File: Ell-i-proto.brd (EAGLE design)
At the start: 99 x 53.3 mm, 145 parts, among them J1 FTDI-SER-6, J10 PJ-102AX, J2 PWMH, J3 PWR, J4 PWML, J5 ANAL, J6 SPI, J7 COMM, J8 ANAH, J9 RJ45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

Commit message: all lines somehow routed and seem to fit to the board, some parts updated, etc
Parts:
- removed Q5: (no value), crystal:SM49
- added C45, C46, C47, C48: 22u, ell-i:0805
- C13: value 10uF -> 22uF; device ell-i:0603 -> ell-i:0805
- C34: value 100uF -> 22u; device rcl:C1206 -> ell-i:0805
- H1, H2, H3, H4, H5, H6: value MOUNT-HOLE3.2 -> MOUNT_HOLE; device holes:3,2 -> ell-i:MOUNT_HOLE
- J1: value FTDI-SER-6 -> TSM-106-01-L-SH; device ell-i:FTDI-SER-6 -> ell-i:TSM-106-01-L-SH
- J10: value PJ-102AX -> KLDX-SMT2-0202; device ell-i:PJ-102A -> ell-i:KLDX-SMT2-0202
- J9: device ell-i:43860-0001 -> ell-i:85502-5008
- S1: value B3SL-10X2P -> EVQQ2/P0; device ell-i:B3SL-10X2P -> ell-i:EVQQ2/P0
- Y1: value 8MHz -> (none); device ell-i:XTAL3225 -> crystal:SM49
- moved PC15 56.4 mm to (68.4, 16.8)
- moved PC14 54.7 mm to (67.3, 17.9)
- moved VPORTN 45.3 mm to (14.5, 19.1)
- moved PC12 44.9 mm to (76.9, 23.4)
- moved V+ 44.6 mm to (16.9, 18.4)
- moved PF5 40.7 mm to (72.3, 6.63)
- moved PF4 39.1 mm to (71.5, 6.93)
- moved TP3 35.9 mm to (33.7, 22.8)
- moved FID2 35.5 mm to (80.9, 38.8)
- moved PB2 30.8 mm to (78.0, 6.73)
- moved R21 30.6 mm to (58.5, 18.4)
- moved D12 28.7 mm to (56.2, 10.1), turned to 270 degrees
- moved C37 28.5 mm to (59.0, 20.0), turned to 90 degrees
- moved C26 24.1 mm to (20.3, 28.0), turned to 180 degrees
- moved TP10 23.4 mm to (4.57, 28.4)
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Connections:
- net +5V: now also C45.1, C46.1, C47.1, C48.1
- net GND: now also J10.1; no longer J10.3
- net GNDI: now also C45.2, C46.2, C47.2, C48.2, J1.6; no longer J1.GND, Y1.2, Y1.4
- net N$6: now also J1.5; no longer J1.-CTS
- net N184903: now also J10.3@1, J10.3@2; no longer J10.1
- net N205481: now also Y1.1; no longer Y1.3
- net NDSR2: now also J1.1; no longer J1.-RTS
- net PE: now also J9.S1, J9.S2
- net PF0: now also Y1.2; no longer Y1.1
- net RX2: now also J1.3; no longer J1.TXD
- net TX2: now also J1.2; no longer J1.RXD
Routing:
- net SCL2: track 0.00 -> 88.3 mm, vias 0 -> 1
- net SDA2: track 0.00 -> 84.5 mm, vias 0 -> 1
- net IO9: track 0.00 -> 73.3 mm, vias 0 -> 3
- net IO8: track 0.00 -> 70.6 mm, vias 0 -> 3
- net RX2: track 23.9 -> 93.7 mm, vias 1 -> 3
- net MOSI1: track 0.00 -> 68.5 mm, vias 0 -> 2
- net SCK1: track 0.00 -> 68.0 mm, vias 0 -> 2
- net MISO1: track 0.00 -> 66.4 mm, vias 0 -> 2
- net IO4: track 0.00 -> 66.0 mm, vias 0 -> 2
- net SCK_ETH: track 0.00 -> 64.3 mm, vias 0 -> 2
- net NSS_ETH: track 0.00 -> 64.2 mm, vias 0 -> 2
- net IO3: track 0.00 -> 63.9 mm, vias 0 -> 2
- net IO7: track 0.00 -> 62.1 mm, vias 0 -> 3
- net IO2: track 0.00 -> 60.5 mm, vias 0 -> 2
- net NRES: track 47.7 -> 107.9 mm, vias 1 -> 8
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- added copper zone on layer 16, net N23620

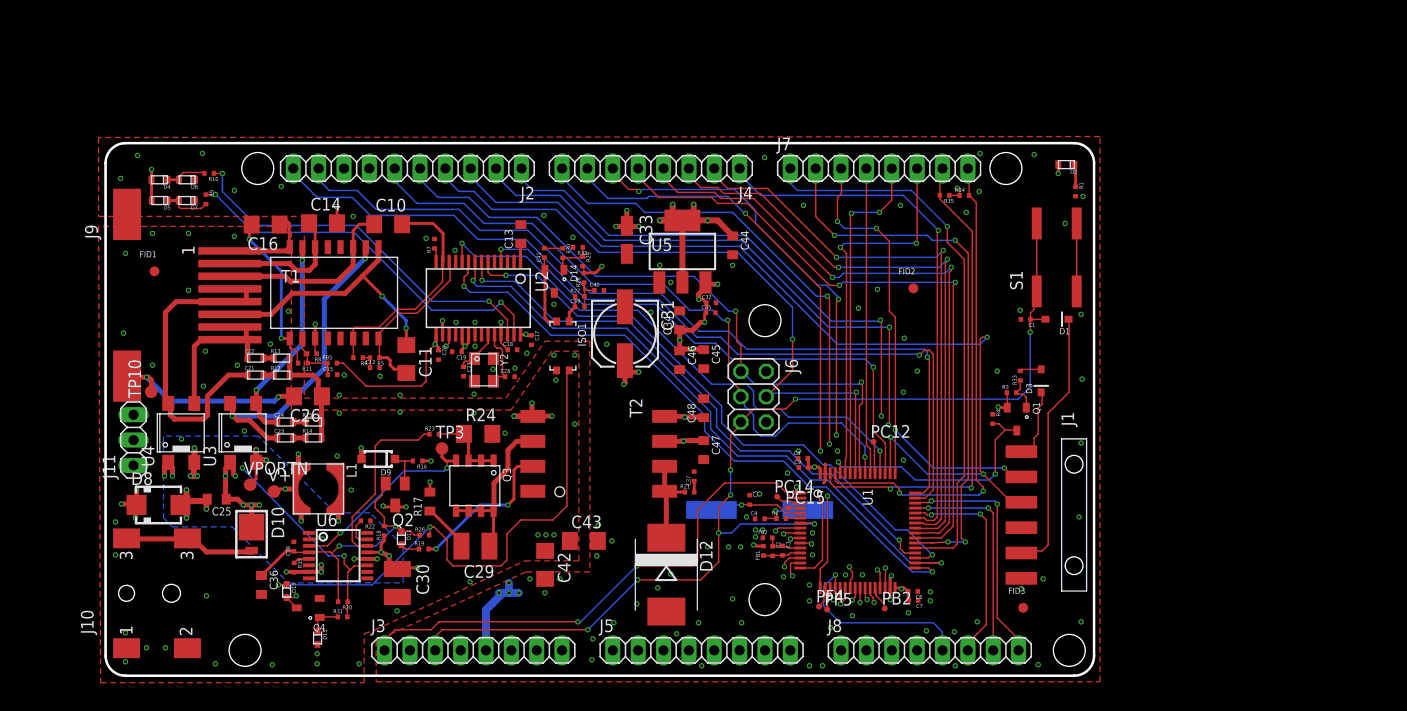
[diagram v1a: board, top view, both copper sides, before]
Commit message: net class & track width updates
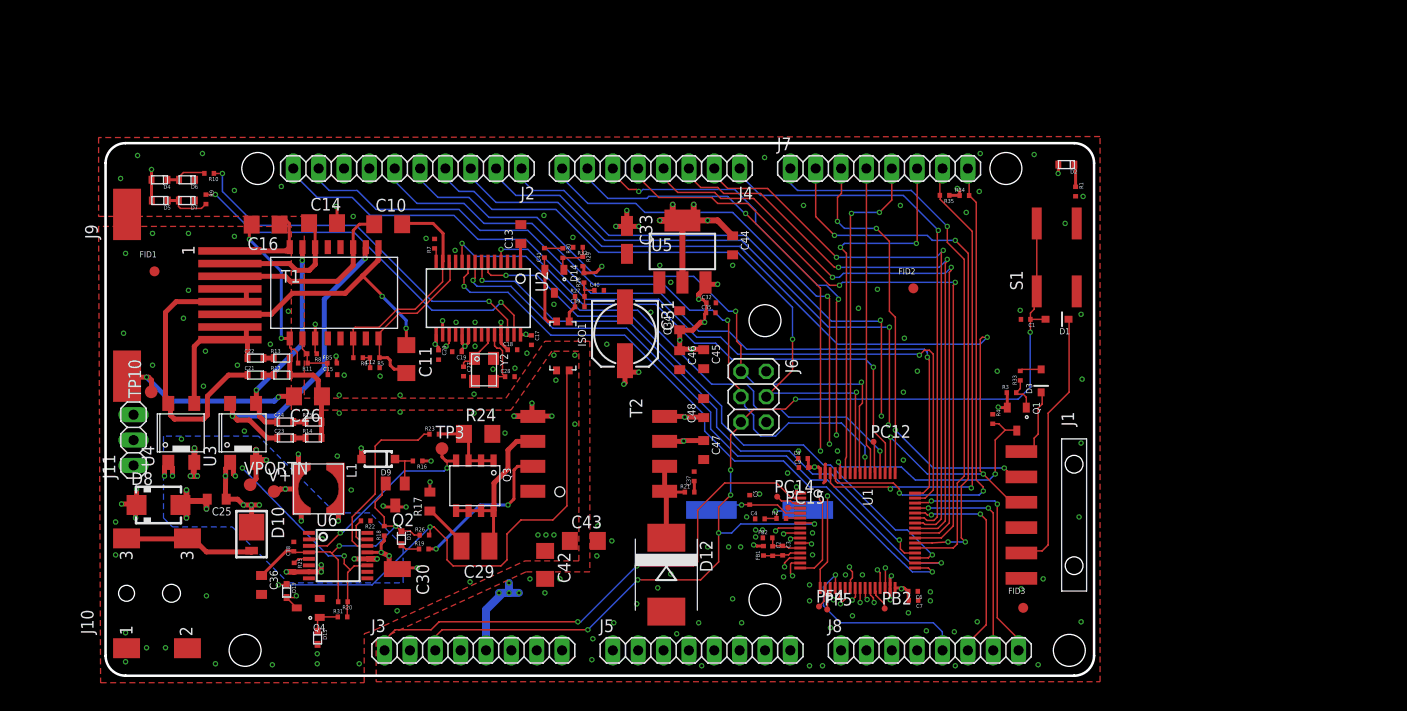
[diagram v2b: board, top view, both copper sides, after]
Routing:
- net +3V3: track 69.6 -> 54.9 mm, vias 19 -> 20
- net GNDI: track 11.0 -> 4.22 mm
- net N23620: track 25.7 -> 24.4 mm
- net GND: vias 40 -> 41

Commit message: gnd planes optimized etc
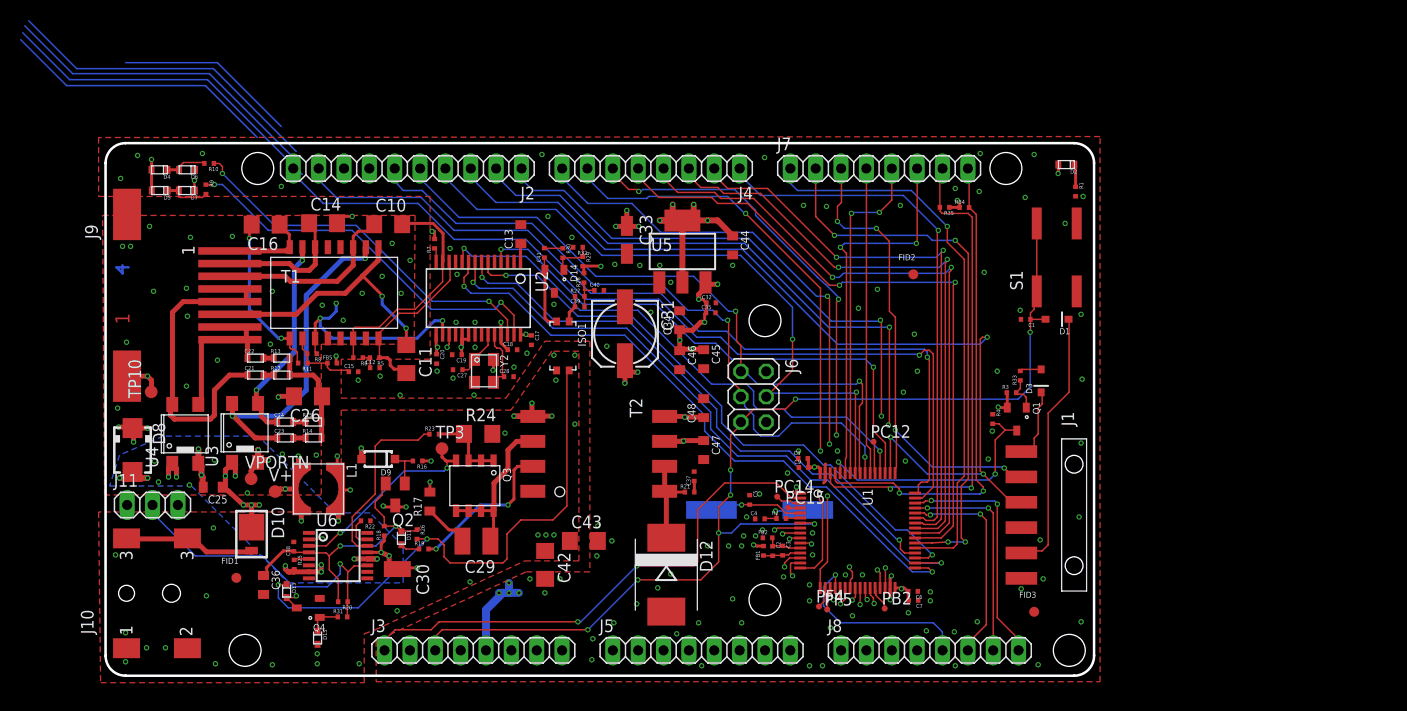
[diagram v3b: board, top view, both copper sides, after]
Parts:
- moved FID1 31.8 mm to (13.1, 9.80)
- moved J11 6.77 mm to (4.70, 17.1), turned to 0 degrees
- moved D8 6.08 mm to (2.70, 22.6), turned to 270 degrees
- moved C15 2.12 mm to (24.8, 30.4)
- moved FID2 1.40 mm to (80.9, 40.2)
- moved C25 1.26 mm to (10.7, 18.9)
- moved R34 1.20 mm to (86.0, 46.9)
- moved R35 1.20 mm to (84.0, 46.9)
- moved FID3 1.17 mm to (93.0, 6.40)
- moved D4 1.00 mm to (5.40, 50.7)
- moved D5 1.00 mm to (5.43, 48.6)
- moved D6 1.00 mm to (8.16, 50.7)
- moved D7 1.00 mm to (8.14, 48.6)
- moved R10 1.00 mm to (10.4, 51.3)
- moved R9 1.00 mm to (10.1, 48.7)
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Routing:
- net RX3: track 0.00 -> 33.9 mm
- net IO11: track 0.00 -> 32.4 mm
- net IO10: track 0.00 -> 32.2 mm
- net MOSI2: track 0.00 -> 27.8 mm
- net IO1: track 0.00 -> 18.3 mm
- net PE: track 19.8 -> 5.40 mm, vias 2 -> 30
- net N08557: track 30.2 -> 33.4 mm, vias 3 -> 4
- net GNDI: track 4.22 -> 7.42 mm, vias 101 -> 111
- net N$10: track 0.00 -> 2.85 mm
- net NPWRGD: track 34.4 -> 32.0 mm, vias 2 -> 1
- net N62909: track 20.2 -> 22.2 mm
- net N12266: track 5.84 -> 7.41 mm
- net SDA1: track 49.0 -> 50.5 mm
- net +3V3: track 54.9 -> 56.4 mm
- net MAG-CT-2: track 32.7 -> 34.2 mm
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- added copper zone on layer 15, net N$4
- added copper zone on layer 2, net N$4
- added copper zone on layer 1, net PE
- added copper zone on layer 15, net PE
- added copper zone on layer 2, net PE
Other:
- board text added: "1"
- board text added: "2"
- board text added: "3"

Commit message: bugfix..
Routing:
- net RX3: track 33.9 -> 0.00 mm
- net IO11: track 32.4 -> 0.00 mm
- net IO10: track 32.2 -> 0.00 mm
- net MOSI2: track 27.8 -> 0.00 mm
- net IO1: track 18.3 -> 0.00 mm
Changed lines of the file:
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@@
 <via x="33.2" y="30.5" extent="1-16" drill="0.3"/>
 <via x="34.8" y="29.8" extent="1-16" drill="0.3"/>
-<wire x1="8.94" y1="48.59" x2="8.9" y2="48.59" width="0.25" layer="1"/>
-<wire x1="8.9" y1="48.59" x2="8.9" y2="49.6" width="0.25" layer="1"/>
+<wire x1="8.94" y1="48.59" x2="8.9" y2="48.59" width="0.3" layer="1"/>
+<wire x1="8.9" y1="48.59" x2="8.9" y2="49.6" width="0.3" layer="1"/>
 </signal>
 <signal name="+5V" class="1">
@@
 </polygon>
 </signal>
-<signal name="IO1">
-<wire x1="17.6" y1="55" x2="11.2" y2="61.4" width="0.15" layer="16"/>
-<wire x1="11.2" y1="61.4" x2="2" y2="61.4" width="0.15" layer="16"/>
-</signal>
-<signal name="IO10">
-<wire x1="-7.7" y1="65.6" x2="-2.9" y2="60.8" width="0.15" layer="16"/>
-<wire x1="-2.9" y1="60.8" x2="10.8" y2="60.8" width="0.15" layer="16"/>
-<wire x1="10.8" y1="60.8" x2="19.1" y2="52.5" width="0.15" layer="16"/>
-</signal>
-<signal name="IO11">
-<wire x1="-8.1" y1="65.1" x2="-3.3" y2="60.3" width="0.15" layer="16"/>
-<wire x1="-3.3" y1="60.3" x2="10.4" y2="60.3" width="0.15" layer="16"/>
-<wire x1="10.4" y1="60.3" x2="18.8" y2="51.9" width="0.15" layer="16"/>
-</signal>
-<signal name="MOSI2">
-<wire x1="-8.5" y1="63.7" x2="-3.9" y2="59.1" width="0.15" layer="16"/>
-<wire x1="-3.9" y1="59.1" x2="10" y2="59.1" width="0.15" layer="16"/>
-<wire x1="10" y1="59.1" x2="15.2" y2="53.9" width="0.15" layer="16"/>
-</signal>
-<signal name="RX3">
-<wire x1="-8.3" y1="64.4" x2="-3.6" y2="59.7" width="0.15" layer="16"/>
-<wire x1="-3.6" y1="59.7" x2="10.2" y2="59.7" width="0.15" layer="16"/>
-<wire x1="10.2" y1="59.7" x2="19.7" y2="50.2" width="0.15" layer="16"/>
-</signal>
 <signal name="N$10">

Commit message: bottom layer filled, DRC nags handled, etc
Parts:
- moved D10 0.55 mm to (14.4, 14.7), turned to 180 degrees
- moved TP10 0.40 mm to (4.57, 28.0)
- moved D4 0.30 mm to (5.70, 50.7)
- moved R10 0.20 mm to (10.6, 51.3)
- moved D5 0.20 mm to (5.63, 48.6)
- moved D6 0.20 mm to (8.36, 50.7)
- moved D7 0.20 mm to (8.34, 48.6)
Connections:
- net N23620 renamed VPORTN
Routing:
- net N184903: track 13.8 -> 11.0 mm
- net N$1: track 5.35 -> 4.36 mm
- net SCL1: track 49.4 -> 50.3 mm
- net +3V3: track 56.4 -> 55.6 mm
- net N62909: track 22.2 -> 23.0 mm
- net N69576: track 54.7 -> 54.0 mm
- net V+: track 31.8 -> 32.5 mm
- net PE: track 5.40 -> 5.79 mm, vias 30 -> 31
- net RX2: track 93.7 -> 93.4 mm, vias 3 -> 4
- net GND: vias 23 -> 25
- added copper zone on layer 16, net GND
- added copper zone on layer 16, net GNDI
- added copper zone on layer 1, net N$4
- added copper zone on layer 16, net N$4
- added copper zone on layer 16, net PE

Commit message: yet more optimization
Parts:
- moved FID1 8.75 mm to (18.6, 3.00)
- moved D11 1.87 mm to (31.2, 14.7), turned to 0 degrees
- moved R22 1.81 mm to (27.6, 14.6), turned to 270 degrees
- moved R23 1.71 mm to (31.2, 24.4)
- moved R26 1.06 mm to (30.8, 13.2)
- moved FID3 0.86 mm to (93.7, 6.90)
- moved R18 0.80 mm to (28.7, 14.5)
- moved R19 0.52 mm to (32.0, 13.2), turned to 270 degrees
- moved D15 0.50 mm to (21.2, 3.29)
- moved C30 0.30 mm to (29.5, 9.28)
- moved C36 0.20 mm to (15.6, 9.09)
- moved R16 0.05 mm to (31.2, 21.5)
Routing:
- net N181699: track 39.2 -> 41.8 mm
- net N181770: track 37.6 -> 40.1 mm
- net N30416: track 10.6 -> 12.7 mm
- net N28455: track 18.2 -> 16.3 mm
- net N27735: track 7.89 -> 9.67 mm
- net RJ45-4-5: track 30.7 -> 32.4 mm
- net N36998: track 3.02 -> 1.57 mm
- net NGATE: track 20.2 -> 21.5 mm
- net N69576: track 54.0 -> 53.2 mm
- net N30229: track 1.94 -> 1.18 mm
- net IO7: track 62.1 -> 61.5 mm
- net VPORTN: track 23.5 -> 24.1 mm
- net N32035: track 3.32 -> 3.82 mm
- net N62909: track 23.0 -> 22.5 mm, vias 13 -> 12
- net GND: track 1.71 -> 1.86 mm, vias 25 -> 31

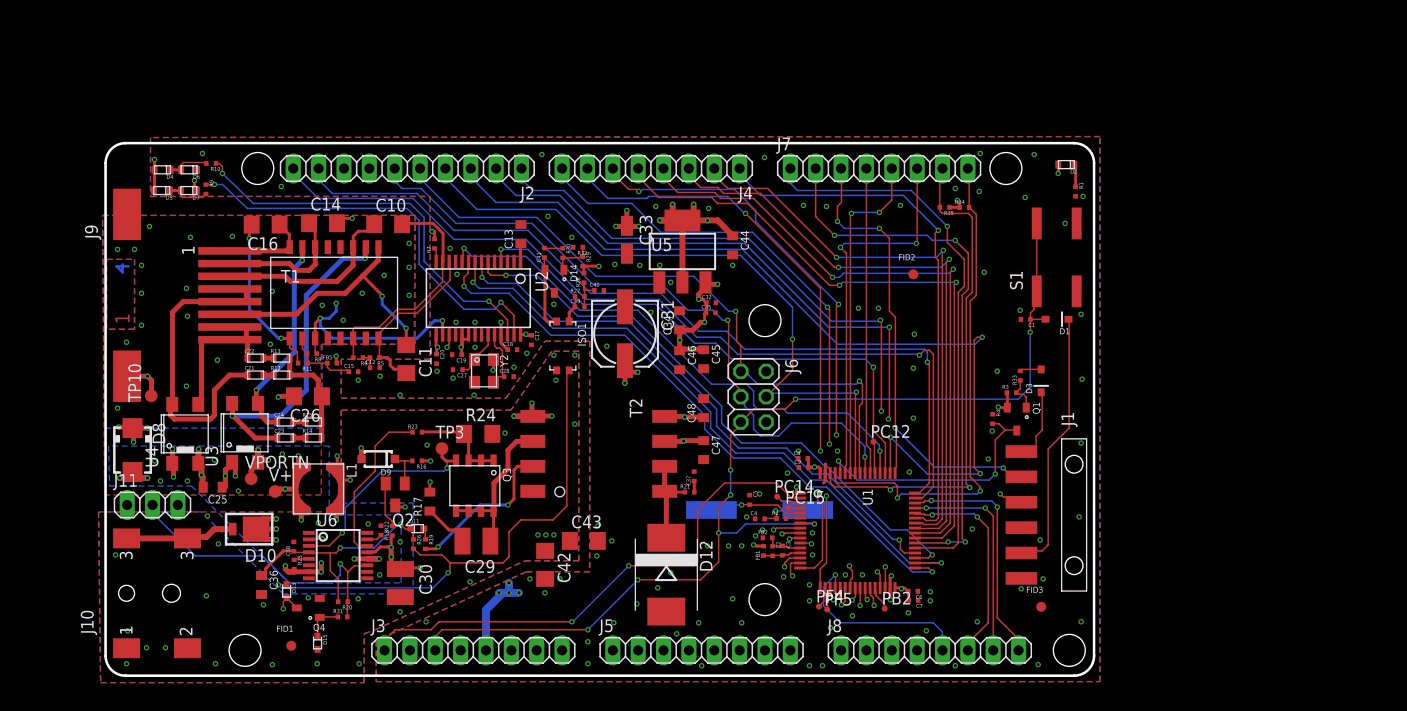
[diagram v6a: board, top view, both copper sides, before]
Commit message: optimizations again, some silks to _tsilk layer
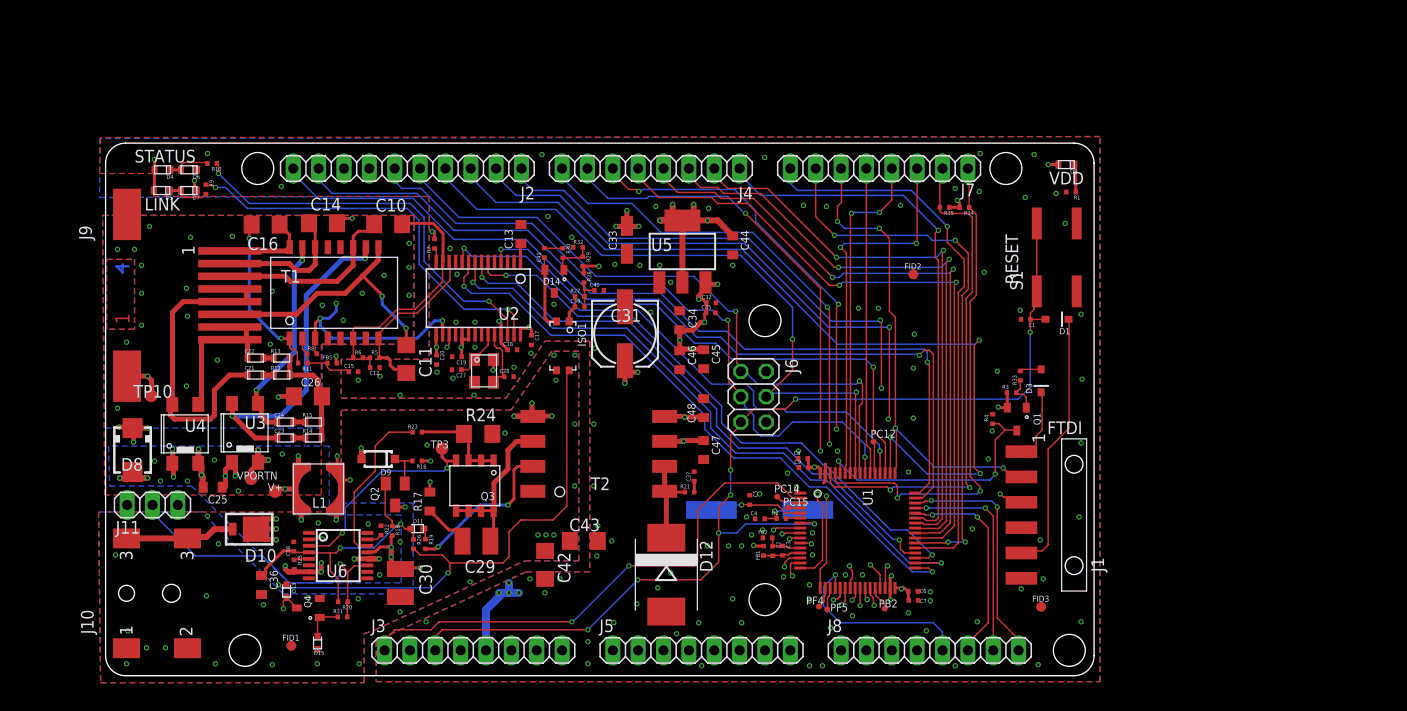
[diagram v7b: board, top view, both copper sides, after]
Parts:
- moved R1 0.46 mm to (96.7, 48.5), turned to 180 degrees
- moved C19 0.20 mm to (35.2, 31.9)
- moved C20 0.10 mm to (33.1, 31.6)
- moved C27 0.10 mm to (35.2, 30.6)
- moved R10 0.10 mm to (10.7, 51.3)
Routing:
- net IO9: track 73.3 -> 77.0 mm
- net RX2: track 93.4 -> 92.2 mm
- net N181699: track 41.8 -> 40.8 mm
- net N41567: track 2.28 -> 2.79 mm
- net GNDI: vias 111 -> 113
- net GND: vias 31 -> 32
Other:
- board text added: "FTDI"
- board text added: "LINK"
- board text added: "RESET"
- board text added: "STATUS"
- board text added: "VDD"

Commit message: Changed 1x6 pinstrip to an FTDI-connector component.
Changed middle layer wires with outer layer wires:

- Under T1
- Left of U6

Optimized away vias for J2 and J4 pins.

Other optimizations.
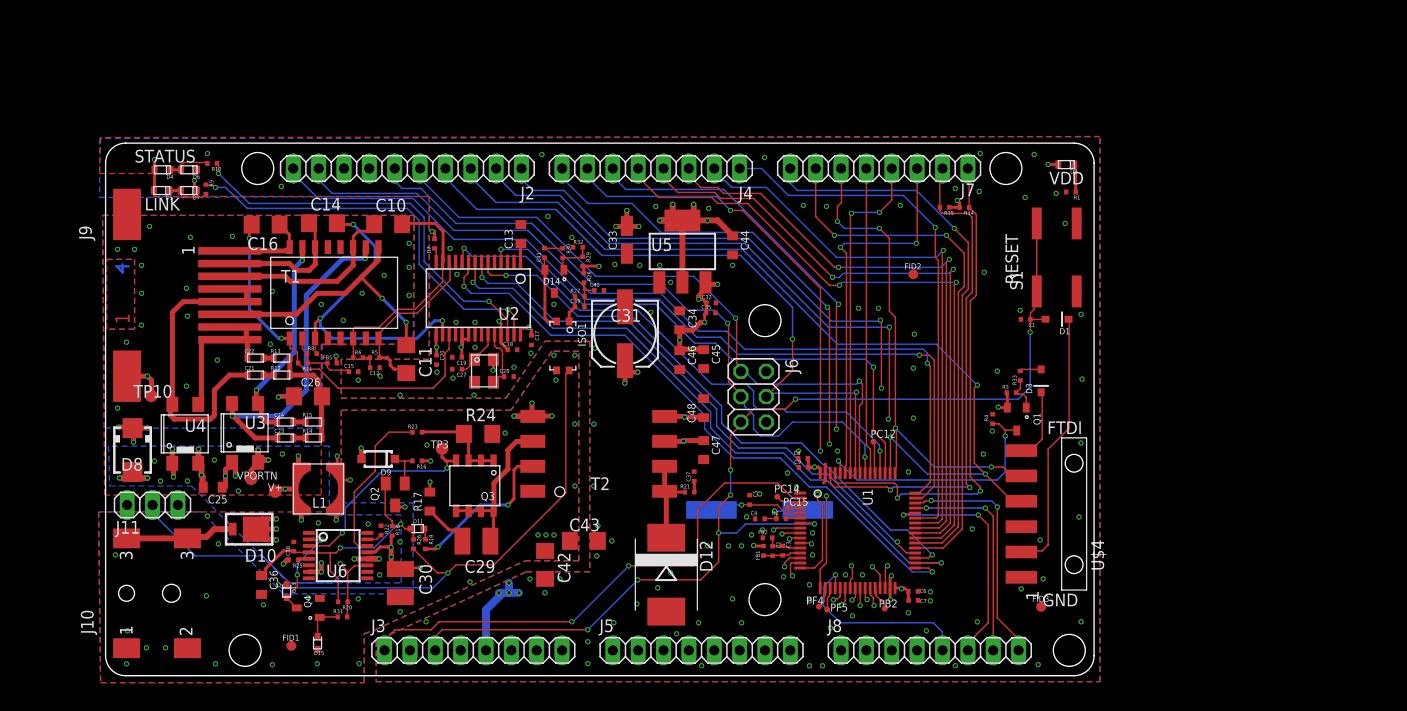
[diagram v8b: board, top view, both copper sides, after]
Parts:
- removed J1: TSM-106-01-L-SH, ell-i:TSM-106-01-L-SH
- added U$4: FTDI-SER-6-HOR2, ell-i:TSM-106-01-L-SH-REV
- moved R25 0.48 mm to (18.8, 11.6), turned to 180 degrees
- moved C27 0.06 mm to (35.2, 30.7)
- moved C19 0.05 mm to (35.2, 31.9)
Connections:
- net GNDI: now also U$4.1; no longer J1.6
- net N$6: now also U$4.2; no longer J1.5
- net NDSR2: now also U$4.6; no longer J1.1
- net RX2: now also U$4.4; no longer J1.3
- net TX2: now also U$4.5; no longer J1.2
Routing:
- net RX2: track 92.2 -> 89.1 mm, vias 4 -> 3
- net VPORTN: track 24.1 -> 21.1 mm
- net N30416: track 12.7 -> 9.93 mm
- net N69576: track 53.2 -> 50.6 mm
- net NCTS1: track 21.2 -> 23.6 mm
- net SPR2: track 56.0 -> 53.9 mm, vias 4 -> 2
- net N08738: track 35.8 -> 37.4 mm, vias 3 -> 2
- net N08557: track 33.1 -> 34.5 mm, vias 4 -> 3
- net RX1: track 54.4 -> 53.5 mm
- net IO5: track 58.7 -> 57.9 mm, vias 4 -> 3
- net SCL2: track 88.1 -> 87.5 mm
- net TX1: track 57.3 -> 57.0 mm, vias 2 -> 1
